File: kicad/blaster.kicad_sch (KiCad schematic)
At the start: 15 parts, among them Q11 IRLML6344, Q12 IRLML6344, Q13 IRLML6344, Q14 IRLML6344, Q15 IRLML6344

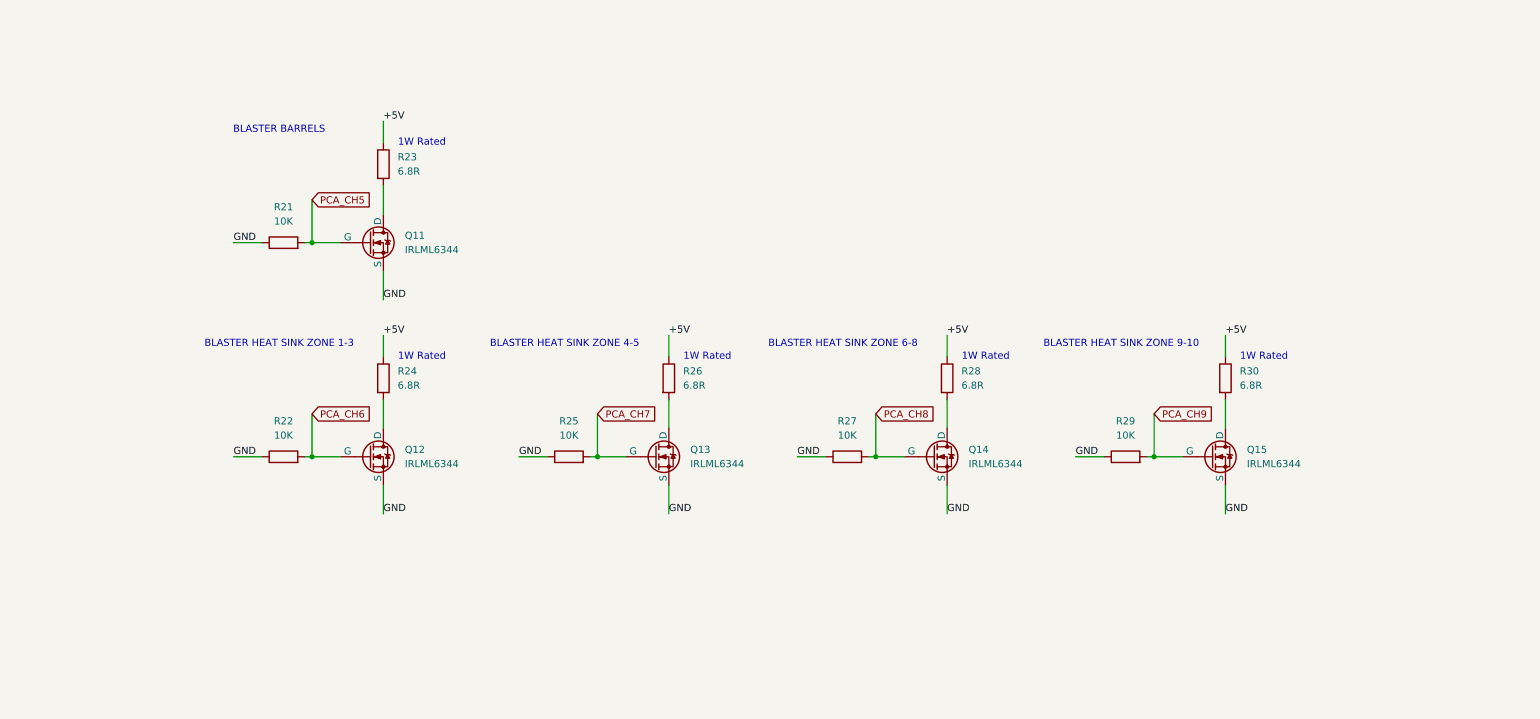
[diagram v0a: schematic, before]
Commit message: feat: blaster schematic update and heatsink sequence prototype (#39)
* feat: add heatsink firing sequence prototype sketch (step-d5)

Co-Authored-By: Claude Sonnet 4.6 <noreply@anthropic.com>

* docs: update wire gauge to Kynar 28 AWG OFHC for all internal wiring

Co-Authored-By: Claude Sonnet 4.6 <noreply@anthropic.com>

* feat: update blaster schematic, channel map, and heatsink sequence

- Reverse heatsink channel order: Ch 1 = front, Ch 5 = rear (reactor end)
- Update blaster.kicad_sch: resistor values, channel labels, zone names
- Regenerate blaster.svg and core-infrastructure.svg from KiCad
- Update docs (blaster.md, channel-map.md, arms.md) to reflect new channel order
- Update step-d5 firmware defines and discharge direction
- Update CLAUDE.md schematic status

Co-Authored-By: Claude Sonnet 4.6 <noreply@anthropic.com>

---------

Co-authored-by: Claude Sonnet 4.6 <noreply@anthropic.com>
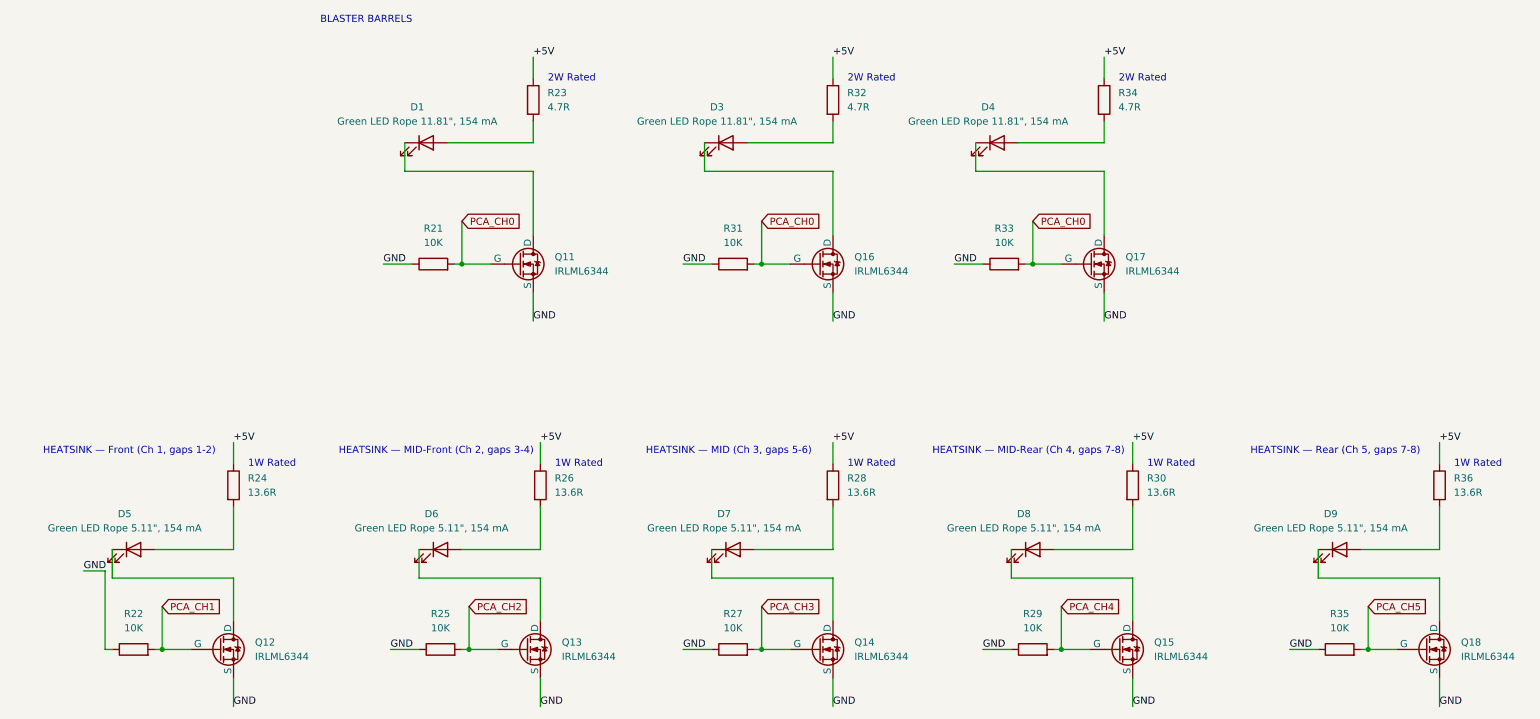
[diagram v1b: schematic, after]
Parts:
- added D1, D3, D4: Green LED Rope 11.81", 154 mA, symbol Device:LED
- added D5, D6, D7, D8, D9: Green LED Rope 5.11", 154 mA, symbol Device:LED
- added Q16, Q17, Q18: IRLML6344, symbol Simulation_SPICE:NMOS
- added R31, R33, R35: 10K, symbol Device:R
- added R32, R34: 4.7R, symbol Device:R
- added R36: 13.6R, symbol Device:R
- R23: value 6.8R -> 4.7R
- R24, R26, R28, R30: value 6.8R -> 13.6R
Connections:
- net +5V: now also R32.1, R34.1, R36.1
- net GND: now also Q16.3 (S), Q17.3 (S), Q18.3 (S), R31.1, R33.1, R35.1
- net PCA_CH5: now also Q18.2 (G), R35.2; no longer Q11.2 (G), R21.2
- net at R24.2: now also D5.2 (A); no longer Q12.1 (D)
- net at Q14.1 (D): now also D7.1 (K); no longer R28.2
- net at R23.2: now also D1.2 (A); no longer Q11.1 (D)
- net at Q15.1 (D): now also D8.1 (K); no longer R30.2
- net at Q13.1 (D): now also D6.1 (K); no longer R26.2
- net PCA_CH6 renamed PCA_CH1
- net PCA_CH7 renamed PCA_CH2
- net PCA_CH8 renamed PCA_CH3
- net PCA_CH9 renamed PCA_CH4
- new net: D4.1 (K), Q17.1 (D)
- new net: D9.2 (A), R36.2
- new net: D3.1 (K), Q16.1 (D)
- new net: D7.2 (A), R28.2
- new net: D1.1 (K), Q11.1 (D)
- new net: D6.2 (A), R26.2
- new net: D3.2 (A), R32.2
- new net: D8.2 (A), R30.2
- new net: D5.1 (K), Q12.1 (D)
- new net: D4.2 (A), R34.2
- new net: D9.1 (K), Q18.1 (D)
- new net PCA_CH0: Q11.2 (G), Q16.2 (G), Q17.2 (G), R21.2, R31.2, R33.2
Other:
- note added: "2W Rated"
- note added: "HEATSINK — Front (Ch 1, gaps 1-2)"
- note added: "HEATSINK — MID (Ch 3, gaps 5-6)"
- note added: "HEATSINK — MID-Front (Ch 2, gaps 3-4)"
- note added: "HEATSINK — MID-Rear (Ch 4, gaps 7-8)"
- note added: "HEATSINK — Rear (Ch 5, gaps 7-8)"
- note removed: "BLASTER HEAT SINK ZONE 1-3"
- note removed: "BLASTER HEAT SINK ZONE 4-5"
- note removed: "BLASTER HEAT SINK ZONE 6-8"
- note removed: "BLASTER HEAT SINK ZONE 9-10"
- moved on the sheet: Q11, Q12, Q13, Q14, Q15, R21, R22, R23, R24, R25, R26, R27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
